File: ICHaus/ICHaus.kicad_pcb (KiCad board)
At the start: 2 copper layers, 85 x 94 mm, 56 parts, among them J1 DB9_Female, J2 DB9_Female, P1 CONN_01X02, P2 CONN_01X02, P3 CONN_01X02, P4 CONN_01X02, P5 CONN_01X02, P6 CONN_01X02, P7 CONN_01X02, P8 CONN_01X02, P9 CONN_01X02, U1 non_plated, U2 non_plated, U3 non_plated, U4 non_plated, U5 IC-NV, U6 am26ls31, U7 SRV05-4, U8 SRV05-4

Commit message: probably final version
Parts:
- added C1: 100n, stmbl:C_0805, F.Cu at (52.8, 106.5)
- added C2: 220p, stmbl:C_0805, F.Cu at (59.4, 107.2)
- added C3: 220p, stmbl:C_0805, F.Cu at (65.0, 107.2)
- added C4: 220p, stmbl:C_0805, F.Cu at (62.2, 107.2)
- added C5: 100n, stmbl:C_0805, F.Cu at (67.8, 107.2)
- added C6: 100n, stmbl:C_0805, F.Cu at (67.6, 92.9)
- added C7: 100n, stmbl:C_0805, F.Cu at (69.5, 92.9)
- added C8: 100n, stmbl:C_0805, F.Cu at (74.2, 96.2)
- added C9: 100n, stmbl:C_0805, F.Cu at (71.4, 92.9)
- added D1: LED, LED_SMD:LED_0603_1608Metric, F.Cu at (62.2, 116.0)
- added J1: DB9_Female, Connector_Dsub:DSUB-9_Female_Horizontal_P2.77x2.84mm_EdgePinOffset7.70mm_Housed_MountingHolesOffset9.12mm, F.Cu at (49.5, 112.0)
- added J2: DB9_Female, Connector_Dsub:DSUB-9_Female_Horizontal_P2.77x2.84mm_EdgePinOffset7.70mm_Housed_MountingHolesOffset9.12mm, F.Cu at (86.5, 112.0)
- added JP1: SolderJumper_2_Open, Jumper:SolderJumper-2_P1.3mm_Open_RoundedPad1.0x1.5mm, B.Cu at (48.8, 106.4)
- added JP10: Jumper_2_Open, Jumper:SolderJumper-2_P1.3mm_Open_RoundedPad1.0x1.5mm, B.Cu at (69.0, 123.0)
- added JP11: SolderJumper_2_Open, Jumper:SolderJumper-2_P1.3mm_Open_RoundedPad1.0x1.5mm, F.Cu at (55.5, 102.5)
- added JP11: SolderJumper_2_Open, Jumper:SolderJumper-2_P1.3mm_Open_RoundedPad1.0x1.5mm, F.Cu at (55.5, 151.5)
- added JP12: SolderJumper_2_Open, Jumper:SolderJumper-2_P1.3mm_Open_RoundedPad1.0x1.5mm, F.Cu at (51.8, 102.5)
- added JP12: SolderJumper_2_Open, Jumper:SolderJumper-2_P1.3mm_Open_RoundedPad1.0x1.5mm, F.Cu at (51.8, 151.5)
- added JP2: SolderJumper_2_Open, Jumper:SolderJumper-2_P1.3mm_Open_RoundedPad1.0x1.5mm, B.Cu at (44.8, 106.5)
- added JP3: SolderJumper_2_Open, Jumper:SolderJumper-2_P1.3mm_Open_RoundedPad1.0x1.5mm, B.Cu at (40.8, 106.4)
- added JP4: SolderJumper_2_Bridged, Jumper:SolderJumper-2_P1.3mm_Bridged_RoundedPad1.0x1.5mm, F.Cu at (39.8, 102.5)
- added JP5: SolderJumper_2_Bridged, Jumper:SolderJumper-2_P1.3mm_Bridged_RoundedPad1.0x1.5mm, F.Cu at (43.8, 102.5)
- added JP6: SolderJumper_2_Bridged, Jumper:SolderJumper-2_P1.3mm_Bridged_RoundedPad1.0x1.5mm, F.Cu at (47.8, 102.5)
- added JP7: Jumper_2_Bridged, Jumper:SolderJumper-2_P1.3mm_Bridged_RoundedPad1.0x1.5mm, F.Cu at (76.5, 93.8)
- added JP8: Jumper_2_Open, Jumper:SolderJumper-2_P1.3mm_Open_RoundedPad1.0x1.5mm, B.Cu at (86.0, 123.0)
- added JP9: Jumper_2_Open, Jumper:SolderJumper-2_P1.3mm_Open_RoundedPad1.0x1.5mm, B.Cu at (77.3, 123.0)
- added P1: CONN_01X02, stmbl:RM3.5_1x2, F.Cu at (32.0, 105.5)
- added P2: CONN_01X02, stmbl:RM3.5_1x2, F.Cu at (39.0, 118.0)
- added P3: CONN_01X02, stmbl:RM3.5_1x2, F.Cu at (47.5, 118.0)
- added P4: CONN_01X02, stmbl:RM3.5_1x2, F.Cu at (56.0, 118.0)
- added P5: CONN_01X02, stmbl:RM3.5_1x2, F.Cu at (32.0, 97.0)
- added P6: CONN_01X02, stmbl:RM3.5_1x2, F.Cu at (69.0, 118.0)
- added P7: CONN_01X02, stmbl:RM3.5_1x2, F.Cu at (93.0, 105.5)
- added P8: CONN_01X02, stmbl:RM3.5_1x2, F.Cu at (77.5, 118.0)
- added P9: CONN_01X02, stmbl:RM3.5_1x2, F.Cu at (86.0, 118.0)
- added POT1: R_POT, Potentiometer_SMD:Potentiometer_Bourns_3214J_Horizontal, F.Cu at (87.8, 86.2)
- added PTC1: JK-SMD0805-035, stmbl:C_0805, F.Cu at (70.5, 107.2)
- added QR*****: Datasheet, ICHaus:QRCoder, B.Cu at (86.8, 90.0)
- added R1: 120, stmbl:C_0805, F.Cu at (54.8, 106.5)
- added R2: R, stmbl:C_0805, F.Cu at (38.8, 106.5)
- added R3: R, stmbl:C_0805, F.Cu at (40.8, 106.5)
- added R4: R, stmbl:C_0805, F.Cu at (42.8, 106.5)
- added R5: R, stmbl:C_0805, F.Cu at (44.8, 106.5)
- added R6: R, stmbl:C_0805, F.Cu at (46.8, 106.5)
- added R7: R, stmbl:C_0805, F.Cu at (48.8, 106.5)
- added R8: 220, stmbl:C_0805, F.Cu at (62.2, 112.5)
- added RCLK1: SolderJumper_3_Open, Jumper:SolderJumper-3_P1.3mm_Bridged12_RoundedPad1.0x1.5mm, F.Cu at (80.2, 85.0)
- added ROT1: SolderJumper_3_Open, Jumper:SolderJumper-3_P1.3mm_Bridged12_RoundedPad1.0x1.5mm, F.Cu at (75.5, 85.0)
- added SF0: SolderJumper_3_Open, Jumper:SolderJumper-3_P1.3mm_Open_RoundedPad1.0x1.5mm_NumberLabels, F.Cu at (70.8, 85.0)
- added SF1: SolderJumper_3_Open, Jumper:SolderJumper-3_P1.3mm_Open_RoundedPad1.0x1.5mm_NumberLabels, F.Cu at (67.0, 85.0)
- added SG0: SolderJumper_3_Open, Jumper:SolderJumper-3_P1.3mm_Open_RoundedPad1.0x1.5mm_NumberLabels, F.Cu at (62.8, 85.0)
- added SG1: SolderJumper_3_Open, Jumper:SolderJumper-3_P1.3mm_Open_RoundedPad1.0x1.5mm_NumberLabels, F.Cu at (59.2, 85.0)
- added U1: non_plated, stmbl:non_plated_3mm, F.Cu at (100.5, 114.0)
- added U2: non_plated, stmbl:non_plated_3mm, F.Cu at (100.5, 89.0)
- added U3: non_plated, stmbl:non_plated_3mm, F.Cu at (24.5, 114.0)
- added U4: non_plated, stmbl:non_plated_3mm, F.Cu at (24.5, 89.0)
- added U5: IC-NV, Package_SO:TSSOP-20_4.4x6.5mm_P0.65mm, F.Cu at (67.5, 100.0)
- added U6: am26ls31, Package_SO:SOIC-16_3.9x9.9mm_P1.27mm, F.Cu at (80.5, 100.0)
- added U7: SRV05-4, Package_TO_SOT_SMD:SOT-23-6, F.Cu at (84.5, 108.0)
- added U8: SRV05-4, Package_TO_SOT_SMD:SOT-23-6, F.Cu at (77.5, 108.0)
- R1: value R -> 120
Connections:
- P2 pad 1: Net-(C2-Pad2) -> Net-(C2-Pad1)
- P2 pad 2: Net-(C2-Pad1) -> Net-(C2-Pad2)
- P3 pad 1: Net-(C3-Pad2) -> Net-(C3-Pad1)
- P3 pad 2: Net-(C3-Pad1) -> Net-(C3-Pad2)
- P4 pad 1: Net-(C4-Pad2) -> Net-(C4-Pad1)
- P4 pad 2: Net-(C4-Pad1) -> Net-(C4-Pad2)
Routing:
- net (no net): track 0.00 -> 1123.2 mm, vias 44 -> 112
- net +5F: track 154.4 -> 174.9 mm
- net Net-(C4-Pad2): track 46.6 -> 54.2 mm, vias 3 -> 4
- net GND: track 27.1 -> 33.6 mm, vias 15 -> 18
- net Net-(C3-Pad2): track 44.3 -> 49.8 mm
- net Net-(C3-Pad1): track 49.6 -> 45.0 mm
- net Net-(C2-Pad2): track 48.4 -> 47.0 mm, vias 1 -> 3
- net Net-(C4-Pad1): track 54.8 -> 55.8 mm, vias 2 -> 3
- added copper zone on B.Cu, net (none)
- added copper zone on F.Cu, net (none)
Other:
- board text added: "JP11-12 Emulate Z-Impulse"

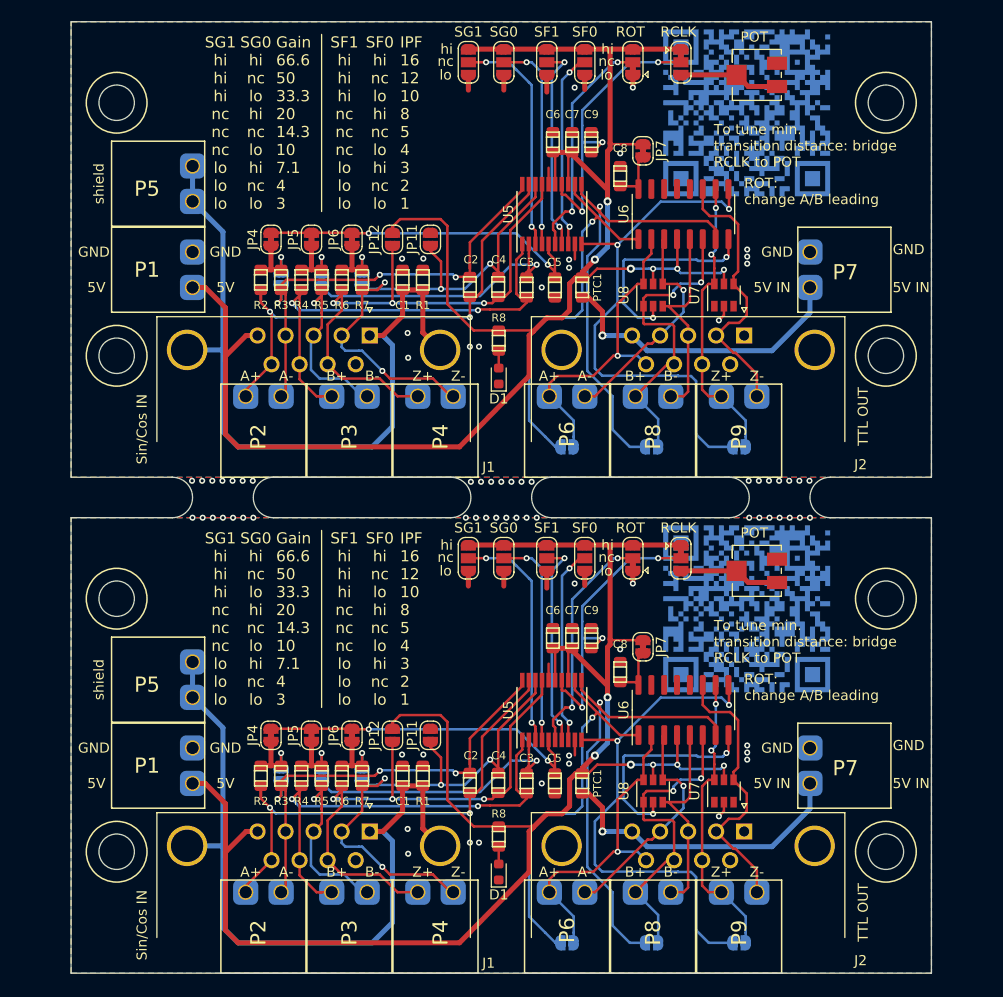
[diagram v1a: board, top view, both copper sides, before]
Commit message: z-detection
added opamp for z impuls detection. (11uass)
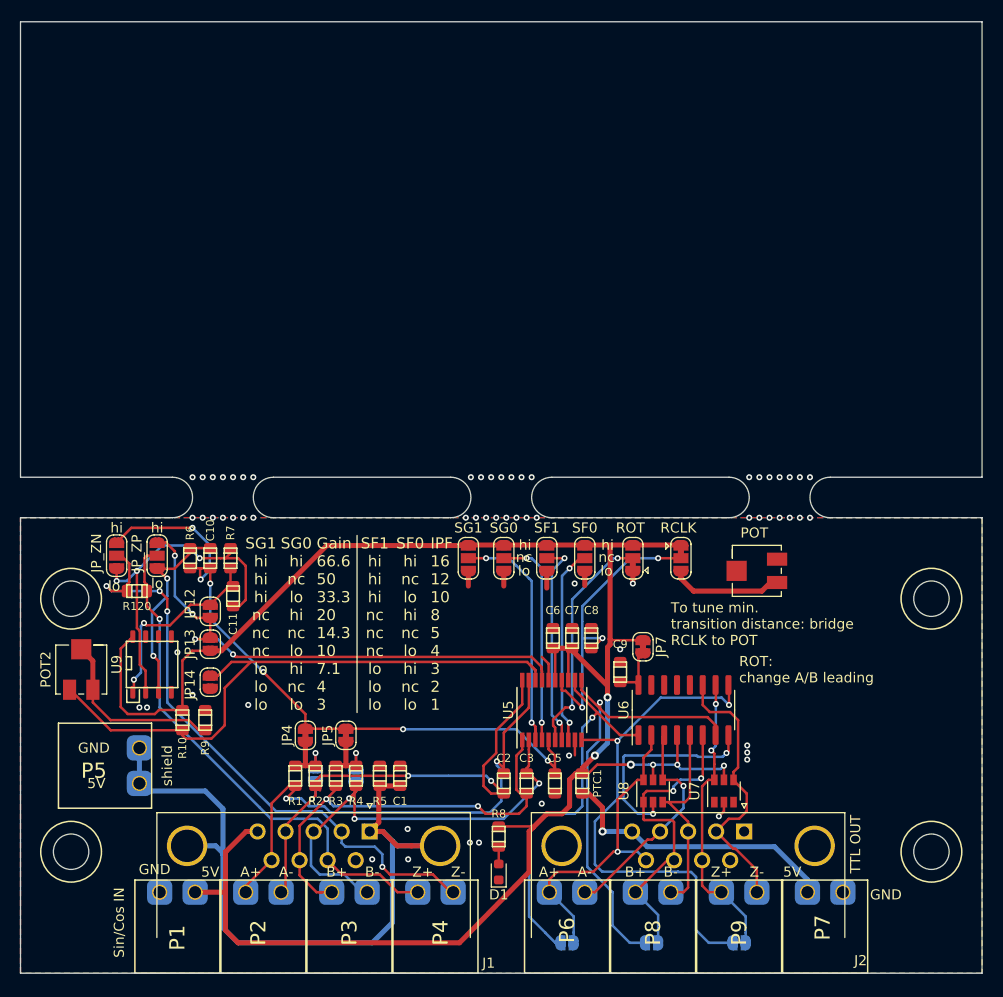
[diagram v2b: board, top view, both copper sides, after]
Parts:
- removed the C1 at (52.8, 106.5)
- removed the C2 at (59.4, 107.2)
- removed the C3 at (65.0, 107.2)
- removed C4: 220p, stmbl:C_0805
- removed the C5 at (67.8, 107.2)
- removed the C6 at (67.6, 92.9)
- removed the C7 at (69.5, 92.9)
- removed the C8 at (74.2, 96.2)
- removed the C9 at (71.4, 92.9)
- removed the D1 at (62.2, 116.0)
- removed the J1 at (49.5, 112.0)
- removed the J2 at (86.5, 112.0)
- removed JP1 (x2), JP11 (x2): SolderJumper_2_Open, Jumper:SolderJumper-2_P1.3mm_Open_RoundedPad1.0x1.5mm
- removed the JP10 at (69.0, 123.0)
- removed the JP12 at (51.8, 102.5)
- removed the JP12 at (51.8, 151.5)
- removed the JP2 at (44.8, 106.5)
- removed the JP3 at (40.8, 106.4)
- removed the JP4 at (39.8, 102.5)
- removed the JP5 at (43.8, 102.5)
- removed JP6 (x2): SolderJumper_2_Bridged, Jumper:SolderJumper-2_P1.3mm_Bridged_RoundedPad1.0x1.5mm
- removed the JP7 at (76.5, 93.8)
- removed the JP8 at (86.0, 123.0)
- removed the JP9 at (77.3, 123.0)
- removed the P1 at (32.0, 105.5)
- removed the P2 at (39.0, 118.0)
- removed the P3 at (47.5, 118.0)
- removed the P4 at (56.0, 118.0)
- removed the P5 at (32.0, 97.0)
- removed the P6 at (69.0, 118.0)
- removed the P7 at (93.0, 105.5)
- removed the P8 at (77.5, 118.0)
- removed the P9 at (86.0, 118.0)
- removed the POT1 at (87.8, 86.2)
- removed the PTC1 at (70.5, 107.2)
- removed QR***** (x2): Datasheet, ICHaus:QRCoder
- removed the R1 at (54.8, 106.5)
- removed the R2 at (38.8, 106.5)
- removed the R3 at (40.8, 106.5)
- removed the R4 at (42.8, 106.5)
- removed the R5 at (44.8, 106.5)
- removed the R6 at (46.8, 106.5)
- removed the R7 at (48.8, 106.5)
- removed the R8 at (62.2, 112.5)
- removed the RCLK1 at (80.2, 85.0)
- removed the ROT1 at (75.5, 85.0)
- removed the SF0 at (70.8, 85.0)
- removed the SF1 at (67.0, 85.0)
- removed the SG0 at (62.8, 85.0)
- removed the SG1 at (59.2, 85.0)
- removed the U1 at (100.5, 114.0)
- removed the U2 at (100.5, 89.0)
- removed the U3 at (24.5, 114.0)
- removed the U4 at (24.5, 89.0)
- removed the U5 at (67.5, 100.0)
- removed the U6 at (80.5, 100.0)
- removed the U7 at (84.5, 108.0)
- removed the U8 at (77.5, 108.0)
- added C11: 220p, stmbl:C_0805, F.Cu at (36.0, 137.8)
- added JP12: SolderJumper_2_Open, Jumper:SolderJumper-2_P1.3mm_Open_RoundedPad1.0x1.5mm, F.Cu at (33.8, 139.2)
- added JP13: SolderJumper_2_Open, Jumper:SolderJumper-2_P1.3mm_Open_RoundedPad1.0x1.5mm, F.Cu at (33.8, 142.5)
- added JP14: SolderJumper_2_Open, Jumper:SolderJumper-2_P1.3mm_Open_RoundedPad1.0x1.5mm, F.Cu at (33.8, 146.2)
- added POT2: 50k, Potentiometer_SMD:Potentiometer_Bourns_3214J_Horizontal, F.Cu at (21.0, 145.0)
- added R10: 25k, stmbl:C_0805, F.Cu at (31.0, 150.0)
- added R120: 120, stmbl:C_0805, F.Cu at (26.5, 137.2)
- added R9: 0, stmbl:C_0805, F.Cu at (33.2, 150.0)
- added SG2: SolderJumper_3_Open, Jumper:SolderJumper-3_P1.3mm_Open_RoundedPad1.0x1.5mm_NumberLabels, F.Cu at (24.5, 133.8)
- added SG3: SolderJumper_3_Open, Jumper:SolderJumper-3_P1.3mm_Open_RoundedPad1.0x1.5mm_NumberLabels, F.Cu at (28.5, 133.8)
- added U9: MCP6001U, stmbl:SOIC-8-N, F.Cu at (28.0, 144.5)
- R5: renamed from R1; value 120 -> 220
- R6: renamed from R7; value R -> 100k
- R7: renamed from R6; value R -> 100k
- moved C10 36.1 mm to (33.8, 134.0)
- moved R6 27.4 mm to (31.8, 134.0), turned to 270 degrees
- moved R7 24.2 mm to (35.8, 134.0)
- moved P1 12.6 mm to (30.5, 167.0), turned to 0 degrees
- moved P7 12.6 mm to (94.5, 167.0), turned to 0 degrees
- moved P5 9.99 mm to (26.8, 154.5)
- moved U1 4.50 mm to (105.0, 163.0)
- moved U2 4.50 mm to (105.0, 138.0)
- moved U3 4.50 mm to (20.0, 163.0)
- moved U4 4.50 mm to (20.0, 138.0)
- moved R5 4.25 mm to (50.5, 155.5)
- moved JP2 3.40 mm to (48.1, 155.5)
- moved JP3 3.40 mm to (44.1, 155.4)
- moved JP4 3.40 mm to (43.1, 151.5)
- moved JP5 3.40 mm to (47.1, 151.5)
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- renumbered C4 to C10, C9 to C8, C8 to C9, R2 to R1, R3 to R2, R4 to R3, R5 to R4
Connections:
- C10 pad 1: Net-(C4-Pad1) -> /VREF
- C10 pad 2: Net-(C4-Pad2) -> Net-(C10-Pad2)
- C5 pad 1: Net-(C5-Pad1) -> /VREF
- J1 pad 2: Net-(C4-Pad2) -> /ZNeg
- J1 pad 7: Net-(C4-Pad1) -> /ZPos
- JP4 pad 2: Net-(C5-Pad1) -> /VREF
- JP5 pad 2: Net-(C5-Pad1) -> /VREF
- P4 pad 1: Net-(C4-Pad1) -> /ZPos
- P4 pad 2: Net-(C4-Pad2) -> /ZNeg
- POT1 pad 2: Net-(POT1-Pad2) -> GND
- POT1 pad 3: Net-(POT1-Pad2) -> Net-(POT1-Pad3)
- R6 pad 1: Net-(C4-Pad2) -> Net-(C10-Pad2)
- R6 pad 2: Net-(JP1-Pad1) -> /VREF
- R7 pad 1: Net-(C4-Pad1) -> Net-(C11-Pad1)
- R7 pad 2: Net-(JP1-Pad1) -> Net-(C11-Pad2)
- RCLK1 pad 3: Net-(POT1-Pad2) -> Net-(POT1-Pad3)
- U5 pad 17: Net-(C4-Pad1) -> /VPosIn
- U5 pad 18: Net-(C4-Pad2) -> /ZNegIn
- U5 pad 5: Net-(C5-Pad1) -> /VREF
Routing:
- net (no net): track 1123.2 -> 0.00 mm, vias 112 -> 43
- net /VREF: track 0.00 -> 68.3 mm, vias 0 -> 6
- net /ZNeg: track 0.00 -> 61.5 mm, vias 0 -> 4
- net /ZNegIn: track 0.00 -> 60.3 mm
- net Net-(C4-Pad1): track 55.8 -> 0.00 mm, vias 3 -> 0
- net Net-(C4-Pad2): track 54.2 -> 0.00 mm, vias 4 -> 0
- net /ZPos: track 0.00 -> 51.6 mm, vias 0 -> 1
- net /VPosIn: track 0.00 -> 51.5 mm, vias 0 -> 4
- net Net-(C11-Pad2): track 0.00 -> 34.7 mm, vias 0 -> 3
- net Net-(C5-Pad1): track 33.8 -> 0.00 mm, vias 2 -> 0
- net +5F: track 174.9 -> 199.9 mm
- net Net-(C10-Pad2): track 0.00 -> 19.9 mm, vias 0 -> 2
- net Net-(C11-Pad1): track 0.00 -> 19.2 mm, vias 0 -> 2
- net Net-(POT2-Pad1): track 0.00 -> 18.7 mm
- net Net-(POT1-Pad3): track 0.00 -> 11.1 mm
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- removed copper zone on B.Cu, net (none)
- removed copper zone on F.Cu, net (none)
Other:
- board size 85 x 94 mm -> 95 x 94 mm
- board text added: "11μAss: R2-4: 25kΩ Gain: 4-7.1 Z: bridge JP12 | JP_ZP/N lo 1VPP: bridge JP1/2 R2,4,120: 120Ω Gain: 3-4 Z: bridge JP_ZP/N hi Z every sin: bridge JP13/14 hi"
- board text added: "11μAss: R2-4: 25kΩ Gain: 4-7.1 Z: bridge JP12 | JP_ZP/N lo 1VPP: bridge JP1/2 R2,4: 120Ω Gain: 3-4 Z: bridge JP_ZP/N hi Z every sin: bridge JP13/14 hi"
- board text added: "JP_ZN"
- board text added: "JP_ZP"
- board text added: "Pins Schirm/GND Z- B- A- 5V GND Z+ B+ A+"
- board text removed: "11μAss: R2-7: 25kΩ Gain: 4-7.1 1VPP: bridge JP1-3 R2,4,6: 120Ω Gain: 3-4"
- board text removed: "5V IN"
- board text removed: "JP11-12 Emulate Z-Impulse"

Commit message: removed unused files
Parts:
- added C1: 100n, stmbl:C_0805, F.Cu at (52.5, 106.5)
- added C10: 220p, stmbl:C_0805, F.Cu at (33.8, 85.0)
- added C11: 220p, stmbl:C_0805, F.Cu at (36.0, 88.8)
- added C2: 220p, stmbl:C_0805, F.Cu at (62.8, 107.2)
- added C3: 220p, stmbl:C_0805, F.Cu at (65.0, 107.2)
- added C5: 100n, stmbl:C_0805, F.Cu at (67.8, 107.2)
- added C6: 100n, stmbl:C_0805, F.Cu at (67.6, 92.9)
- added C7: 100n, stmbl:C_0805, F.Cu at (69.5, 92.9)
- added C8: 100n, stmbl:C_0805, F.Cu at (71.4, 92.9)
- added C9: 100n, stmbl:C_0805, F.Cu at (74.2, 96.2)
- added D1: LED, LED_SMD:LED_0603_1608Metric, F.Cu at (62.2, 116.0)
- added J1: DB9_Female, Connector_Dsub:DSUB-9_Female_Horizontal_P2.77x2.84mm_EdgePinOffset7.70mm_Housed_MountingHolesOffset9.12mm, F.Cu at (49.5, 112.0)
- added J2: DB9_Female, Connector_Dsub:DSUB-9_Female_Horizontal_P2.77x2.84mm_EdgePinOffset7.70mm_Housed_MountingHolesOffset9.12mm, F.Cu at (86.5, 112.0)
- added JP10: Jumper_2_Open, Jumper:SolderJumper-2_P1.3mm_Open_RoundedPad1.0x1.5mm, B.Cu at (69.0, 123.0)
- added JP12: SolderJumper_2_Open, Jumper:SolderJumper-2_P1.3mm_Open_RoundedPad1.0x1.5mm, F.Cu at (33.8, 90.2)
- added JP13: SolderJumper_2_Open, Jumper:SolderJumper-2_P1.3mm_Open_RoundedPad1.0x1.5mm, F.Cu at (33.8, 93.5)
- added JP14: SolderJumper_2_Open, Jumper:SolderJumper-2_P1.3mm_Open_RoundedPad1.0x1.5mm, F.Cu at (33.8, 97.2)
- added JP2: SolderJumper_2_Open, Jumper:SolderJumper-2_P1.3mm_Open_RoundedPad1.0x1.5mm, B.Cu at (48.1, 106.5)
- added JP3: SolderJumper_2_Open, Jumper:SolderJumper-2_P1.3mm_Open_RoundedPad1.0x1.5mm, B.Cu at (44.1, 106.4)
- added JP4: SolderJumper_2_Bridged, Jumper:SolderJumper-2_P1.3mm_Bridged_RoundedPad1.0x1.5mm, F.Cu at (43.1, 102.5)
- added JP5: SolderJumper_2_Bridged, Jumper:SolderJumper-2_P1.3mm_Bridged_RoundedPad1.0x1.5mm, F.Cu at (47.1, 102.5)
- added JP7: Jumper_2_Bridged, Jumper:SolderJumper-2_P1.3mm_Bridged_RoundedPad1.0x1.5mm, F.Cu at (76.5, 93.8)
- added JP8: Jumper_2_Open, Jumper:SolderJumper-2_P1.3mm_Open_RoundedPad1.0x1.5mm, B.Cu at (86.0, 123.0)
- added JP9: Jumper_2_Open, Jumper:SolderJumper-2_P1.3mm_Open_RoundedPad1.0x1.5mm, B.Cu at (77.3, 123.0)
- added P1: CONN_01X02, stmbl:RM3.5_1x2, F.Cu at (30.5, 118.0)
- added P2: CONN_01X02, stmbl:RM3.5_1x2, F.Cu at (39.0, 118.0)
- added P3: CONN_01X02, stmbl:RM3.5_1x2, F.Cu at (47.5, 118.0)
- added P4: CONN_01X02, stmbl:RM3.5_1x2, F.Cu at (56.0, 118.0)
- added P5: CONN_01X02, stmbl:RM3.5_1x2, F.Cu at (26.8, 105.5)
- added P6: CONN_01X02, stmbl:RM3.5_1x2, F.Cu at (69.0, 118.0)
- added P7: CONN_01X02, stmbl:RM3.5_1x2, F.Cu at (94.5, 118.0)
- added P8: CONN_01X02, stmbl:RM3.5_1x2, F.Cu at (77.5, 118.0)
- added P9: CONN_01X02, stmbl:RM3.5_1x2, F.Cu at (86.0, 118.0)
- added POT1: R_POT, Potentiometer_SMD:Potentiometer_Bourns_3214J_Horizontal, F.Cu at (87.8, 86.2)
- added POT2: 50k, Potentiometer_SMD:Potentiometer_Bourns_3214J_Horizontal, F.Cu at (21.0, 96.0)
- added PTC1: JK-SMD0805-035, stmbl:C_0805, F.Cu at (70.5, 107.2)
- added R1: R, stmbl:C_0805, F.Cu at (42.1, 106.5)
- added R10: 25k, stmbl:C_0805, F.Cu at (31.0, 101.0)
- added R120: 120, stmbl:C_0805, F.Cu at (26.5, 88.2)
- added R2: R, stmbl:C_0805, F.Cu at (44.1, 106.5)
- added R3: R, stmbl:C_0805, F.Cu at (46.1, 106.5)
- added R4: R, stmbl:C_0805, F.Cu at (48.1, 106.5)
- added R5: 220, stmbl:C_0805, F.Cu at (50.5, 106.5)
- added R6: 100k, stmbl:C_0805, F.Cu at (31.8, 85.0)
- added R7: 100k, stmbl:C_0805, F.Cu at (35.8, 85.0)
- added R8: 220, stmbl:C_0805, F.Cu at (62.2, 112.5)
- added R9: 0, stmbl:C_0805, F.Cu at (33.2, 101.0)
- added RCLK1: SolderJumper_3_Open, Jumper:SolderJumper-3_P1.3mm_Bridged12_RoundedPad1.0x1.5mm, F.Cu at (80.2, 85.0)
- added ROT1: SolderJumper_3_Open, Jumper:SolderJumper-3_P1.3mm_Bridged12_RoundedPad1.0x1.5mm, F.Cu at (75.5, 85.0)
- added SF0: SolderJumper_3_Open, Jumper:SolderJumper-3_P1.3mm_Open_RoundedPad1.0x1.5mm_NumberLabels, F.Cu at (70.8, 85.0)
- added SF1: SolderJumper_3_Open, Jumper:SolderJumper-3_P1.3mm_Open_RoundedPad1.0x1.5mm_NumberLabels, F.Cu at (67.0, 85.0)
- added SG0: SolderJumper_3_Open, Jumper:SolderJumper-3_P1.3mm_Open_RoundedPad1.0x1.5mm_NumberLabels, F.Cu at (62.8, 85.0)
- added SG1: SolderJumper_3_Open, Jumper:SolderJumper-3_P1.3mm_Open_RoundedPad1.0x1.5mm_NumberLabels, F.Cu at (59.2, 85.0)
- added SG2: SolderJumper_3_Open, Jumper:SolderJumper-3_P1.3mm_Open_RoundedPad1.0x1.5mm_NumberLabels, F.Cu at (24.5, 84.8)
- added SG3: SolderJumper_3_Open, Jumper:SolderJumper-3_P1.3mm_Open_RoundedPad1.0x1.5mm_NumberLabels, F.Cu at (28.5, 84.8)
- added U1: non_plated, stmbl:non_plated_3mm, F.Cu at (105.0, 114.0)
- added U2: non_plated, stmbl:non_plated_3mm, F.Cu at (105.0, 89.0)
- added U3: non_plated, stmbl:non_plated_3mm, F.Cu at (20.0, 114.0)
- added U4: non_plated, stmbl:non_plated_3mm, F.Cu at (20.0, 89.0)
- added U5: IC-NV, Package_SO:TSSOP-20_4.4x6.5mm_P0.65mm, F.Cu at (67.5, 100.0)
- added U6: am26ls31, Package_SO:SOIC-16_3.9x9.9mm_P1.27mm, F.Cu at (80.5, 100.0)
- added U7: SRV05-4, Package_TO_SOT_SMD:SOT-23-6, F.Cu at (84.5, 108.0)
- added U8: SRV05-4, Package_TO_SOT_SMD:SOT-23-6, F.Cu at (77.5, 108.0)
- added U9: MCP6001U, stmbl:SOIC-8-N, F.Cu at (28.0, 95.5)
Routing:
- net (no net): track 0.00 -> 790.6 mm, vias 43 -> 128
- added copper zone on F.Cu, net (none)
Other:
- board text removed: "11μAss: R2-4: 25kΩ Gain: 4-7.1 Z: bridge JP12 | JP_ZP/N lo 1VPP: bridge JP1/2 R2,4: 120Ω Gain: 3-4 Z: bridge JP_ZP/N hi Z every sin: bridge JP13/14 hi"
- board text removed: "Pins GND/Schirm Z- B- A- 5V GND Z+ B+ A+"
